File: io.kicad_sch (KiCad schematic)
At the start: 29 parts, among them J3 DE-9SA-J4-2R, SW1 SW_DIP_x08, U12 8255A, U13 SN74HCT138N, U19 TL16C550BN, U20 CD74HCT30E, U21 MAX232, U22 MAX232, Y2 1.8432MHZ

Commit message: PIC controller added
Signed-off-by: Lucy Mielke <user@domain.tld>
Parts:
- added C35: 0.1uF, Capacitor_THT:C_Disc_D3.0mm_W1.6mm_P2.50mm, symbol Device:C
- added R12: 10k, Resistor_THT:R_Axial_DIN0204_L3.6mm_D1.6mm_P5.08mm_Horizontal, symbol Device:R
- added U23: 8259A, Package_DIP:DIP-28_W15.24mm_Socket, symbol Interface:8259A
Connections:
- net 5V: now also C35.1, R12.1, U23.28 (VCC)
- net GND: now also C35.2, U23.14 (GND)
- net IORC: now also U23.3 (~{RD})
- net IOWC: now also U23.2 (~{WR})
- net PIC_CS: now also U23.1 (~{CS})
- net UART_IRQ: now also U23.22 (IR4)
- net addr0: now also U23.27 (A0)
- net d0: now also U23.11 (D0)
- net d1: now also U23.10 (D1)
- net d2: now also U23.9 (D2)
- net d3: now also U23.8 (D3)
- net d4: now also U23.7 (D4)
- net d5: now also U23.6 (D5)
- net d6: now also U23.5 (D6)
- net d7: now also U23.4 (D7)
- new net: R12.2, U23.16 (~{SP}/~{EN})
- new net 8253_8254_IRQ: U23.18 (IR0)
- new net INTA: U23.26 (~{INTA})
- new net INTR: U23.17 (INT)
- new net ISA0_IRQ: U23.20 (IR2)
- new net ISA1_IRQ: U23.23 (IR5)
- new net ISA2_IRQ: U23.24 (IR6)
- new net ISA3_IRQ: U23.25 (IR7)
- new net PS2_IRQ: U23.19 (IR1)
- new net RTL_IRQ: U23.21 (IR3)
- no-connect marks 6 -> 9
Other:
- note added: "IO Controller"
- note added: "UART/RS232 Serial"
- moved on the sheet: C26, C27, C28, C31, C32, J3, U22

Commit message: reorganise
Signed-off-by: Lucy Mielke <user@domain.tld>
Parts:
- removed C21, C22, C25, C26: 0.1uF, Capacitor_THT:C_Disc_D3.0mm_W1.6mm_P2.50mm, symbol Device:C
- removed C23, C24: 20pF, Capacitor_THT:C_Disc_D3.0mm_W1.6mm_P2.50mm, symbol Device:C
- removed C27, C28, C29, C30, C31, C32, C33, C34: 1uF, Capacitor_THT:C_Disc_D3.0mm_W1.6mm_P2.50mm, symbol Device:C
- removed J3: DE-9SA-J4-2R, Connector_Dsub:DSUB-9_Socket_Horizontal_P2.77x2.84mm_EdgePinOffset7.70mm_Housed_MountingHolesOffset9.12mm, symbol Connector:DE9_Socket_MountingHoles
- removed R10, R11, R9: 10k, Resistor_THT:R_Axial_DIN0204_L3.6mm_D1.6mm_P5.08mm_Horizontal, symbol Device:R
- removed U19: TL16C550BN, Package_DIP:DIP-40_W15.24mm_Socket, symbol Interface_UART:16550
- removed U20: CD74HCT30E, footprints:N14, symbol CD74HCT30E:CD74HCT30E
- removed U21, U22: MAX232, Package_DIP:DIP-16_W7.62mm_Socket, symbol Interface_UART:MAX232
- removed Y2: 1.8432MHZ, Crystal:Crystal_HC49-U_Vertical, symbol Device:Crystal
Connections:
- no-connect marks 9 -> 7
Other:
- added sheet RS232 UART (io_rs232_uart.kicad_sch)
- note added: "Programmable Interrupt Controller"
- note removed: "UART/RS232 Serial"
- moved on the sheet: C35, R12, U23

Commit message: add PIT
Signed-off-by: Lucy Mielke <user@domain.tld>
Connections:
- net PB0: now reaches U12.18 (PB0)
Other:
- added sheet Programmable Interrupt Timer (io_pit.kicad_sch)
- sheet RS232 UART ports: added UART_IRQ; removed none

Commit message: PS/2 Controller and connections
Signed-off-by: Lucy Mielke <user@domain.tld>
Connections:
- net PS2_CS: now reaches U13.11 (Y4)
- net ISA0_IRQ renamed PS2_MOUSE_IRQ
- net PS2_IRQ renamed PS2_KBD_IRQ
- no-connect marks 7 -> 6
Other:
- added sheet PS2 (io_ps2.kicad_sch)
- moved on the sheet: C35, R12, U23

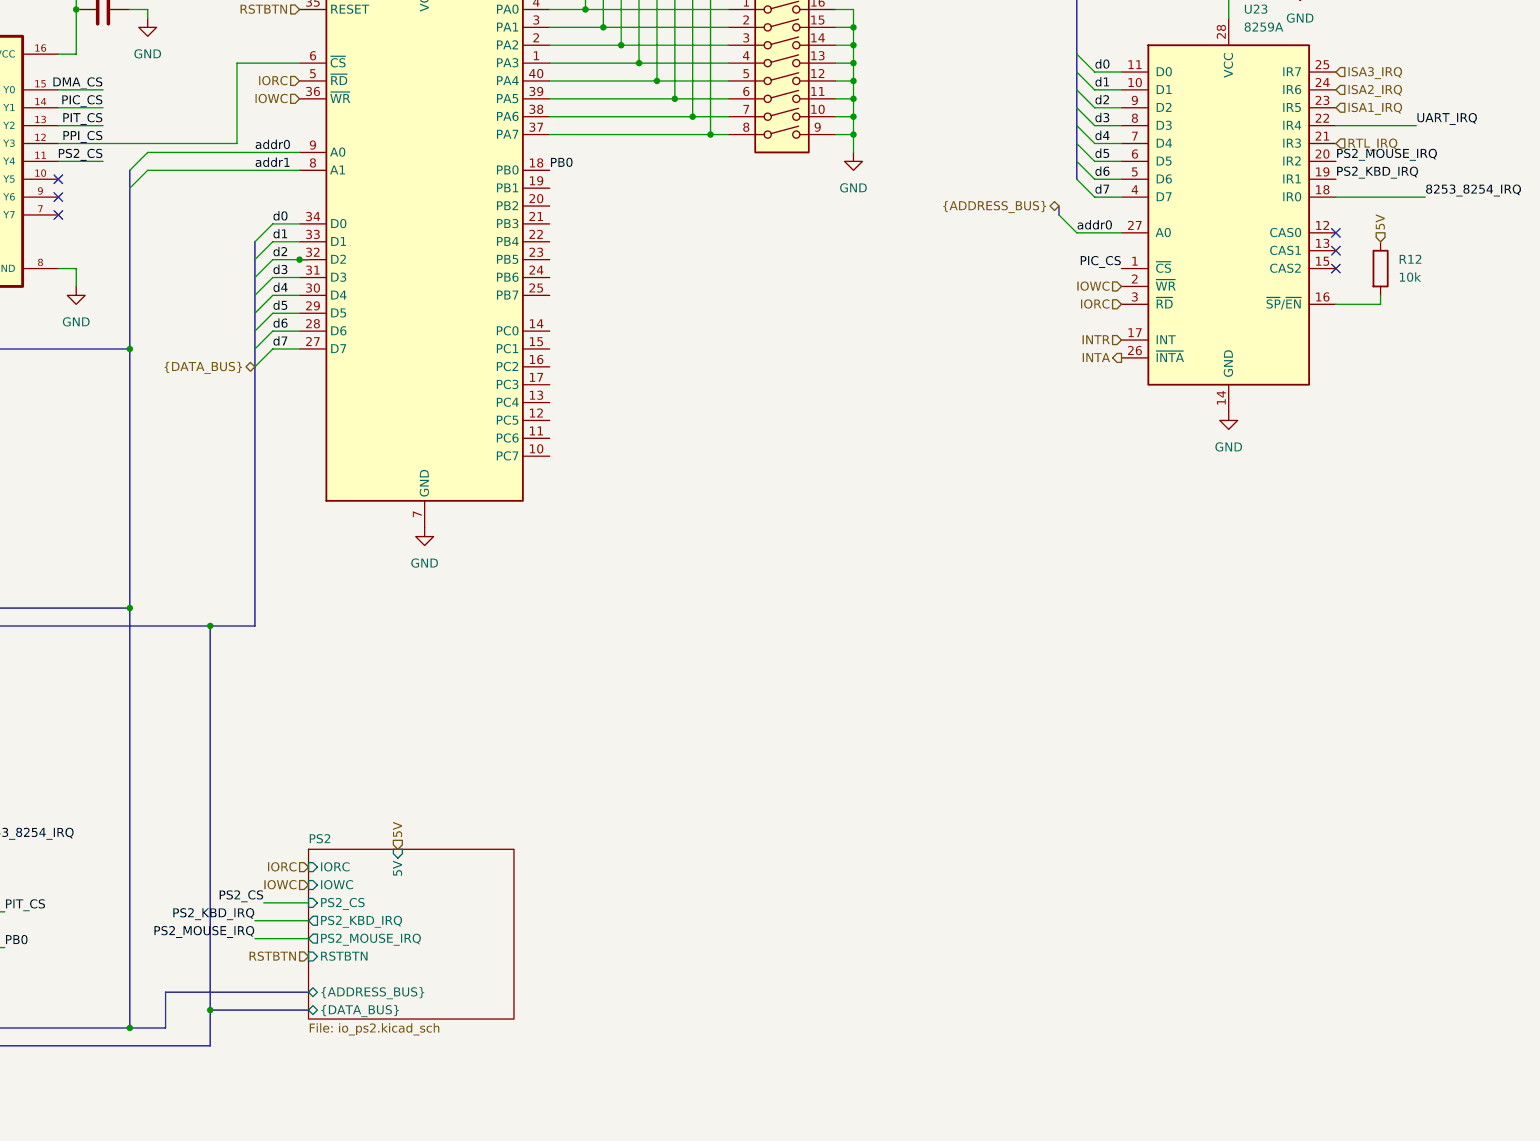
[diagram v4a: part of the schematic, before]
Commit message: Added compatible RJ45 Ethernet
Signed-off-by: Lucy Mielke <user@domain.tld>
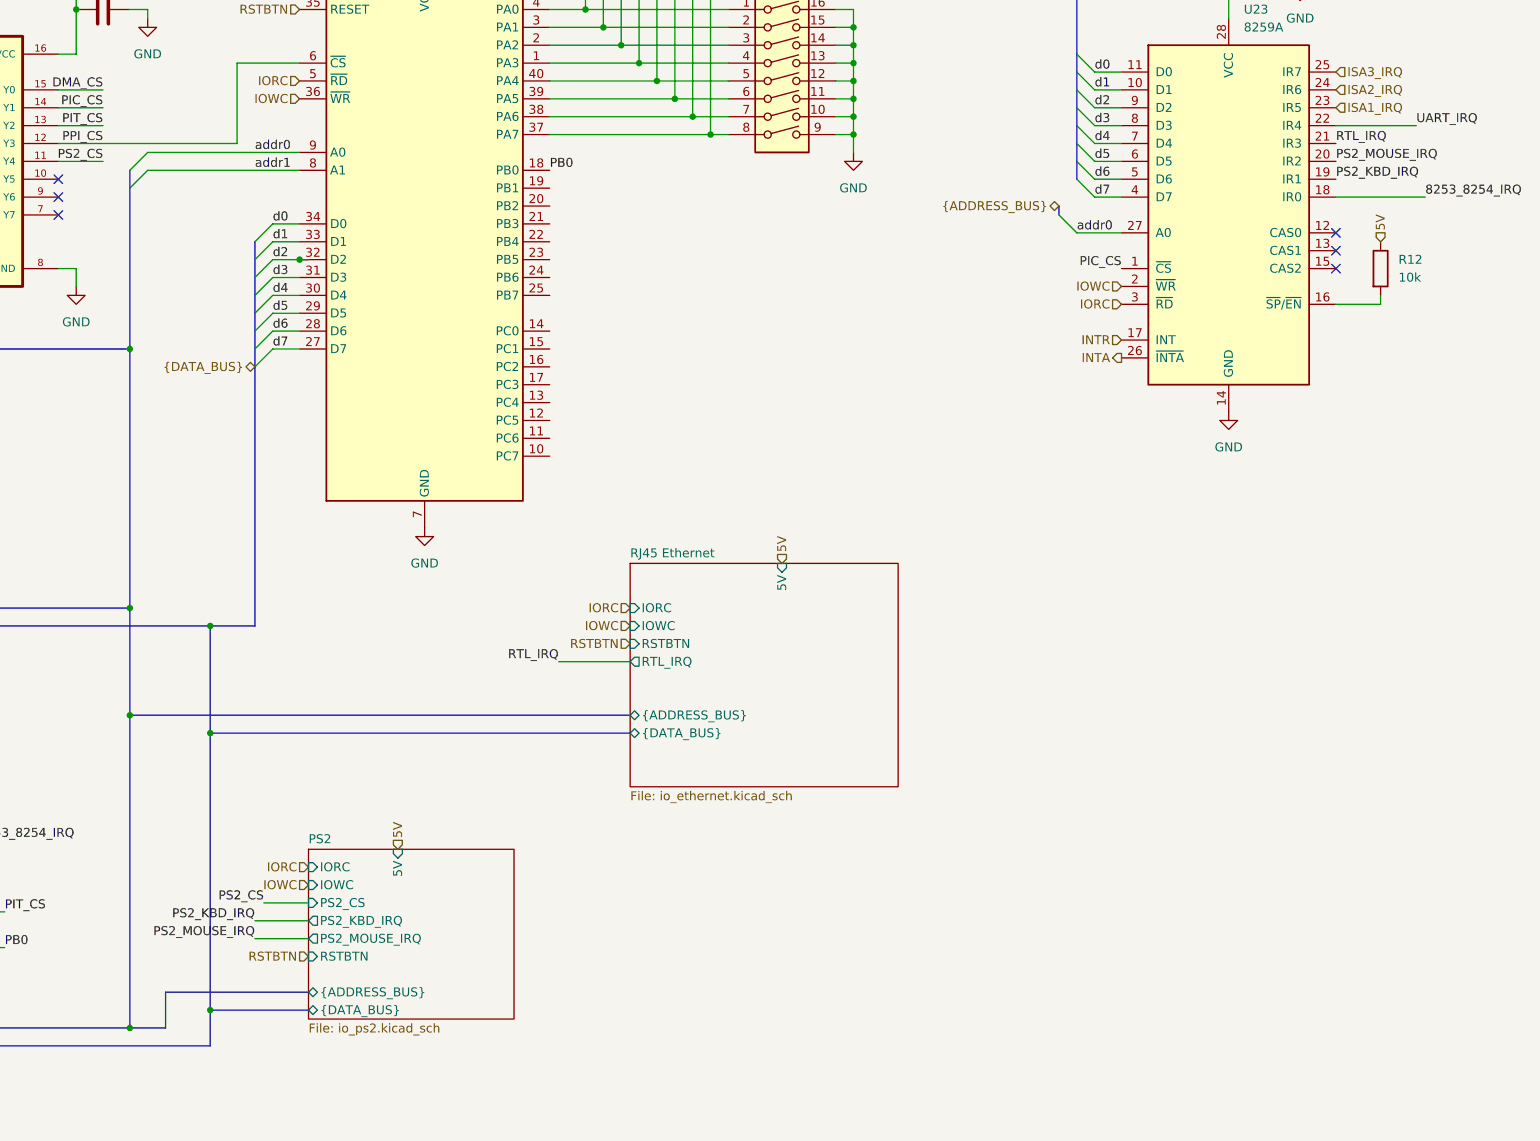
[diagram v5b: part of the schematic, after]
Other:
- added sheet RJ45 Ethernet (io_ethernet.kicad_sch)
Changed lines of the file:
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@@
 	)
 	(junction
+		(at 80.01 137.16)
+		(diameter 0)
+		(color 0 0 0 0)
+	)
+	(junction
 		(at 182.88 49.53)
 		(diameter 0)
@@
 	)
 	(junction
+		(at 91.44 139.7)
+		(diameter 0)
+		(color 0 0 0 0)
+	)
+	(junction
 		(at 182.88 46.99)
 		(diameter 0)
@@
 		)
 	)
+	(bus
+		(pts
+			(xy 151.13 137.16) (xy 80.01 137.16)
+		)
+		(stroke
+			(width 0)
+			(type default)
+		)
+	)
 	(wire
 		(pts
@@
 	(bus
 		(pts
+			(xy 91.44 139.7) (xy 151.13 139.7)
+		)
+		(stroke
+			(width 0)
+			(type default)
+		)
+	)
+	(bus
+		(pts
 			(xy 80.01 121.92) (xy 80.01 85.09)
 		)
@@
 	(wire
 		(pts
+			(xy 140.97 129.54) (xy 151.13 129.54)
+		)
+		(stroke
+			(width 0)
+			(type default)
+		)
+	)
+	(wire
+		(pts
 			(xy 217.17 45.72) (xy 220.98 45.72)
 		)
@@
 	(bus
 		(pts
-			(xy 80.01 121.92) (xy 80.01 181.61)
+			(xy 80.01 121.92) (xy 80.01 137.16)
 		)
 		(stroke
@@
 	(bus
 		(pts
-			(xy 91.44 124.46) (xy 91.44 179.07)
+			(xy 91.44 124.46) (xy 91.44 139.7)
 		)
 		(stroke
@@
 		)
 	)
+	(bus
+		(pts
+			(xy 91.44 139.7) (xy 91.44 179.07)
+		)
+		(stroke
+			(width 0)
+			(type default)
+		)
+	)
 	(wire
 		(pts
@@
 		)
 	)
+	(bus
+		(pts
+			(xy 80.01 137.16) (xy 80.01 181.61)
+		)
+		(stroke
+			(width 0)
+			(type default)
+		)
+	)
 	(wire
 		(pts
@@
 		)
 	)
+	(label "RTL_IRQ"
+		(at 251.46 55.88 0)
+		(effects
+			(font
+				(size 1.27 1.27)
+			)
+			(justify left bottom)
+		)
+	)
 	(label "addr8"
 		(at 27.94 50.8 0)
@@
 		)
 	)
+	(label "RTL_IRQ"
+		(at 140.97 129.54 180)
+		(effects
+			(font
+				(size 1.27 1.27)
+			)
+			(justify right bottom)
+		)
+	)
 	(label "d6"
 		(at 100.33 82.55 0)
@@
 		)
 	)
+	(hierarchical_label "RSTBTN"
+		(shape input)
+		(at 151.13 127 180)
+		(effects
+			(font
+				(size 1.27 1.27)
+			)
+			(justify right)
+		)
+	)
 	(hierarchical_label "5V"
 		(shape input)
@@
 		)
 	)
+	(hierarchical_label "IORC"
+		(shape input)
+		(at 151.13 121.92 180)
+		(effects
+			(font
+				(size 1.27 1.27)
+			)
+			(justify right)
+		)
+	)
 	(hierarchical_label "PCLK"
 		(shape input)
@@
 		)
 	)
+	(hierarchical_label "IOWC"
+		(shape input)
+		(at 151.13 124.46 180)
+		(effects
+			(font
+				(size 1.27 1.27)
+			)
+			(justify right)
+		)
+	)
 	(hierarchical_label "ISA1_IRQ"
 		(shape input)
@@
 	(hierarchical_label "5V"
 		(shape input)
-		(at 15.24 53.34 90)
+		(at 172.72 115.57 90)
 		(effects
 			(font
@@
 		)
 	)
-	(hierarchical_label "RTL_IRQ"
+	(hierarchical_label "5V"
 		(shape input)
-		(at 251.46 55.88 0)
+		(at 15.24 53.34 90)
 		(effects
 			(font
@@
 				)
 			)
+		)
+	)
+	(sheet
+		(at 151.13 115.57)
+		(size 38.1 31.75)
+		(exclude_from_sim no)
+		(in_bom yes)
+		(on_board yes)
+		(dnp no)
+		(fields_autoplaced yes)
+		(stroke
+			(width 0.1524)
+			(type solid)
+		)
+		(fill
+			(color 0 0 0 0)
+		)
+		(property "Sheetname" "RJ45 Ethernet"
+			(at 151.13 114.8584 0)
+			(show_name no)
+			(do_not_autoplace no)
+			(effects
+				(font
+					(size 1.27 1.27)
+				)
+				(justify left bottom)
+			)
+		)
+		(property "Sheetfile" "io_ethernet.kicad_sch"
+			(at 151.13 147.9046 0)
+			(show_name no)
+			(do_not_autoplace no)
+			(effects
+				(font
+					(size 1.27 1.27)
+				)
+				(justify left top)
+			)
+		)
+		(pin "5V" input
+			(at 172.72 115.57 90)
+			(effects
+				(font
+					(size 1.27 1.27)
+				)
+				(justify right)
+			)
+		)
+		(pin "IORC" input
+			(at 151.13 121.92 180)
+			(effects
+				(font
+					(size 1.27 1.27)
+				)
+				(justify left)
+			)
+		)
+		(pin "IOWC" input
+			(at 151.13 124.46 180)
+			(effects
+				(font
+					(size 1.27 1.27)
+				)
+				(justify left)
+			)
+		)
+		(pin "RSTBTN" input
+			(at 151.13 127 180)
+			(effects
+				(font
+					(size 1.27 1.27)
+				)
+				(justify left)
+			)
+		)
+		(pin "RTL_IRQ" output
+			(at 151.13 129.54 180)
+			(effects
+				(font
+					(size 1.27 1.27)
+				)
+				(justify left)
+			)
+		)
+		(pin "{ADDRESS_BUS}" bidirectional
+			(at 151.13 137.16 180)
+			(effects
+				(font
+					(size 1.27 1.27)
+				)
+				(justify left)
+			)
+		)
+		(pin "{DATA_BUS}" bidirectional
+			(at 151.13 139.7 180)
+			(effects
+				(font
+					(size 1.27 1.27)
+				)
+				(justify left)
+			)
+		)
+		(instances
+			(project "scarlet-8088"
+				(path "/6bf7a8bc-eb70-43f6-b16b-1b538dd0d96d/c2b4fe32-c8e2-4470-a0ad-251842fa1d08"
+					(page "9")
+				)
+			)

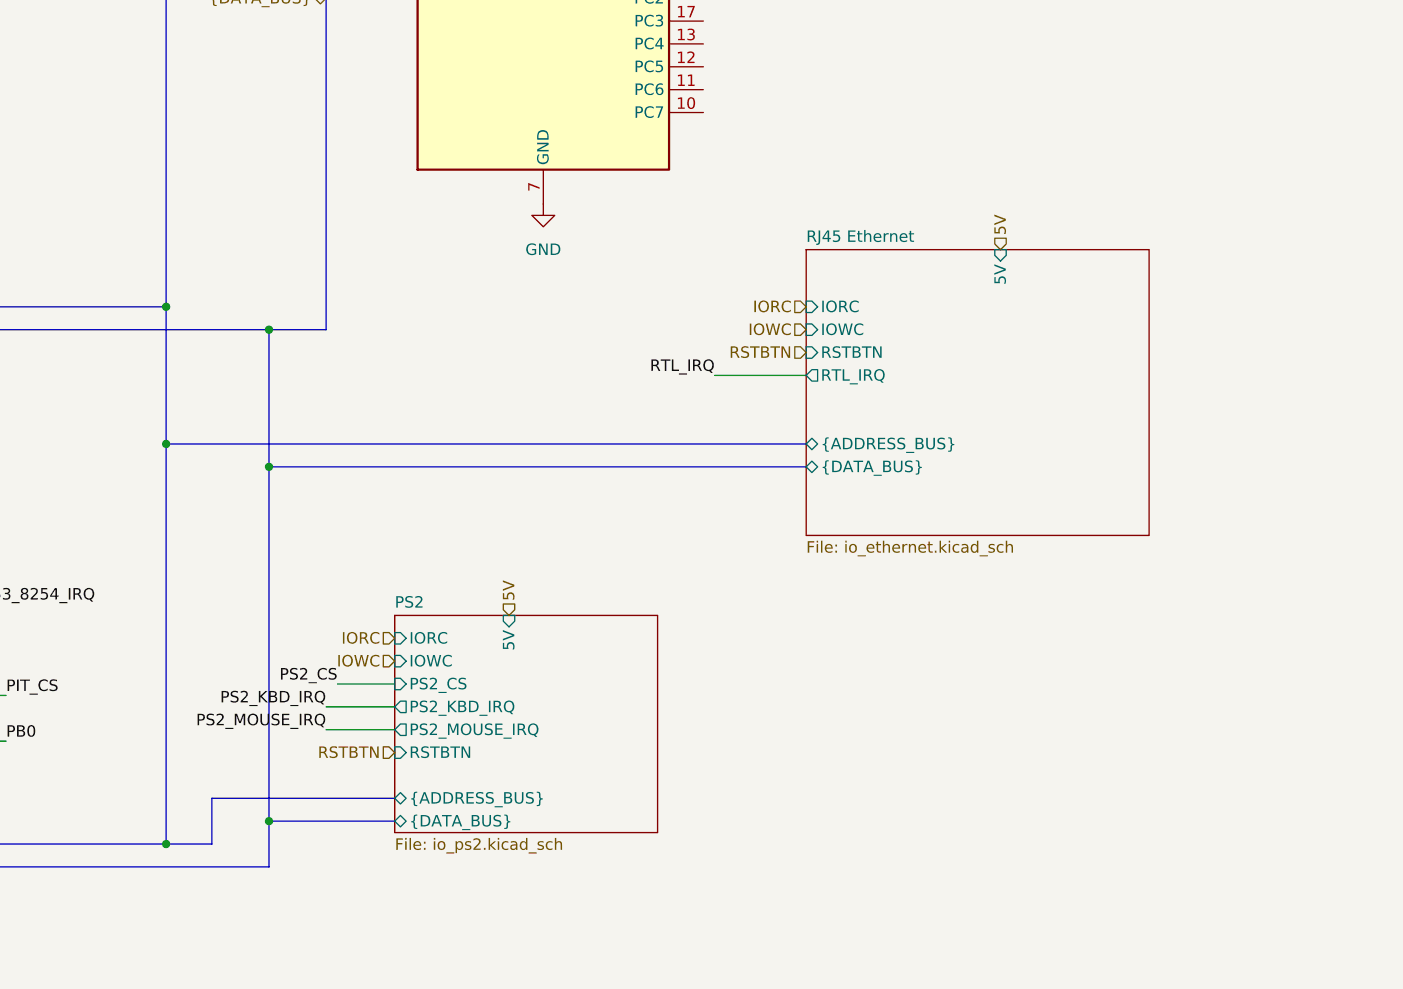
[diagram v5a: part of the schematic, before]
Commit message: IDE controller/connector
Signed-off-by: Lucy Mielke <user@domain.tld>
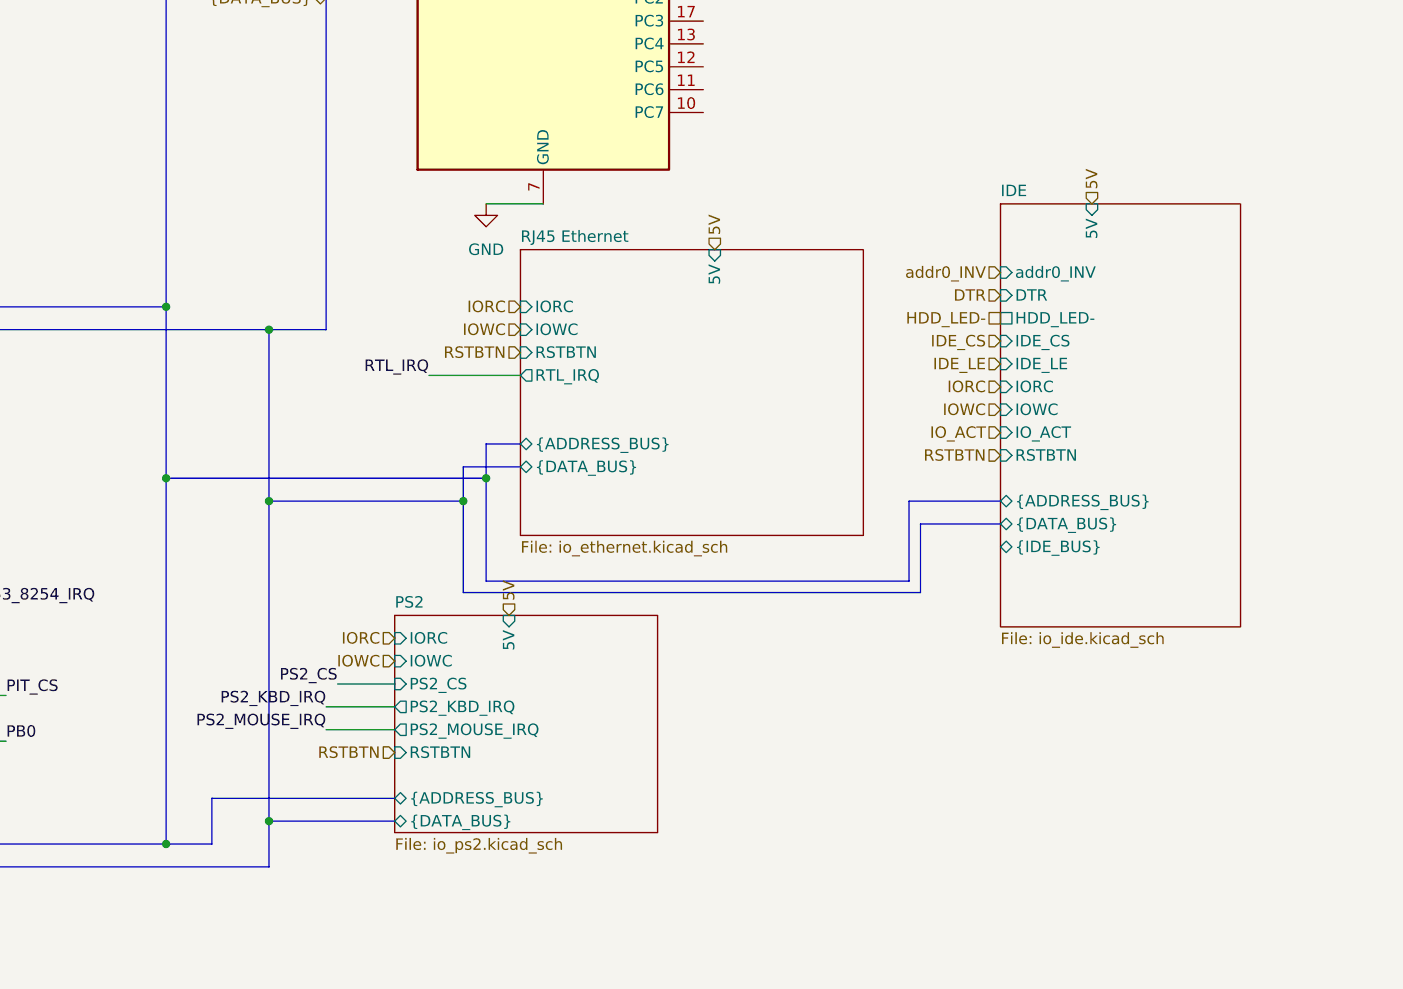
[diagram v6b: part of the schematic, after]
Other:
- added sheet IDE (io_ide.kicad_sch)
